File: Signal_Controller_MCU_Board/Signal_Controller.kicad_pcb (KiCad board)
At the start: 2 copper layers, 65 x 75 mm, 53 parts, among them J1 BARREL_JACK, J2 USB_OTG, J3 CONN_02X03, J4 CONN_01X03, J5 CONN_01X02, J6 CONN_01X02, J8 CONN_01X07, Q1 2N7002P,215, Q2 2N7002P,215, Q3 2N7002P,215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

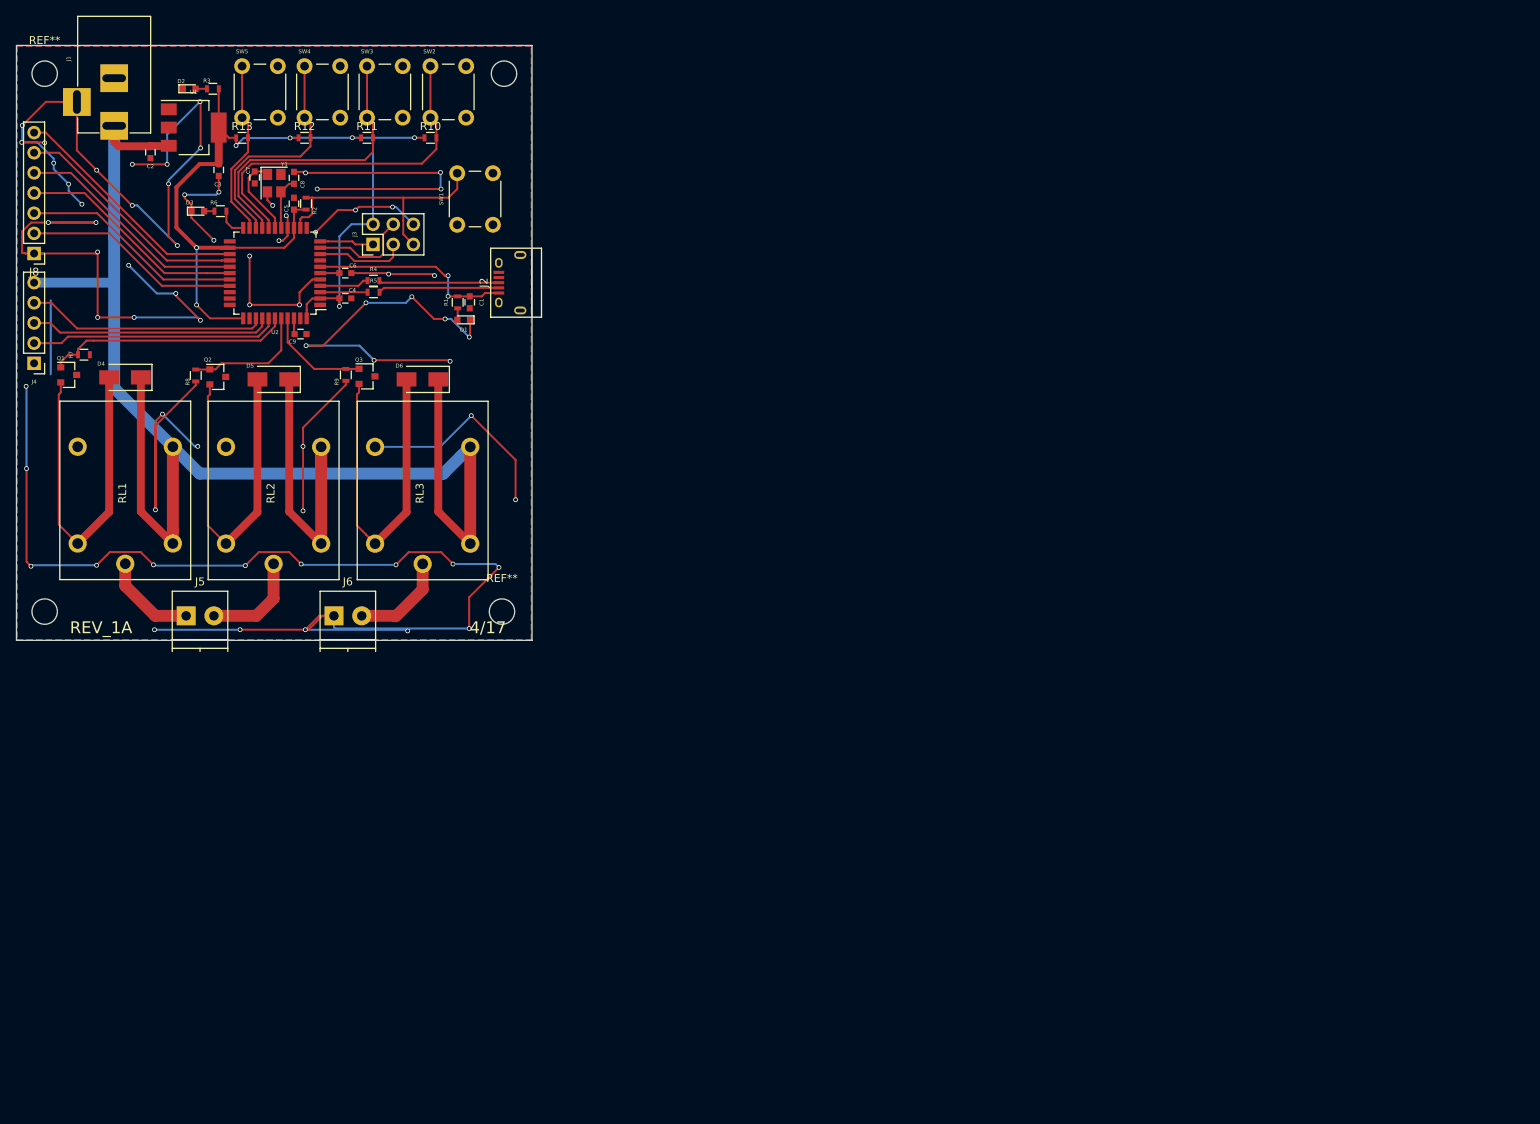
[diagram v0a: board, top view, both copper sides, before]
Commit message: Both boards mostly completed
just need final tweaks, silkscreen stuff etc, all major routing and
placement done
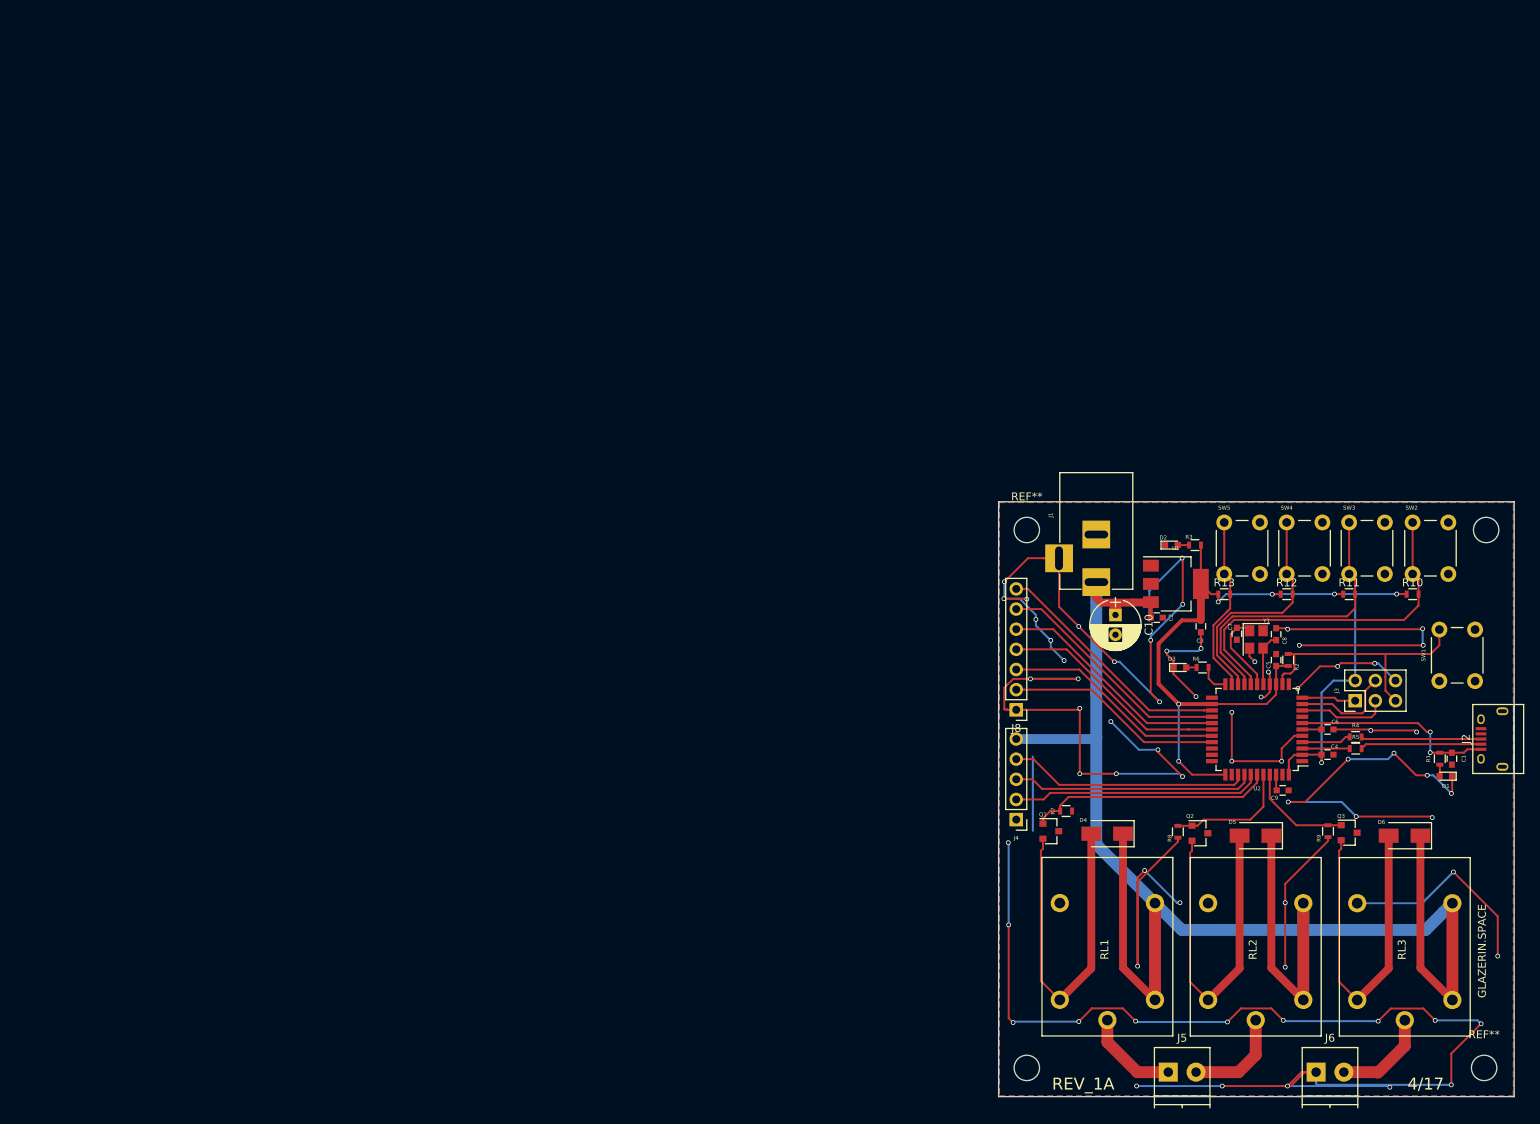
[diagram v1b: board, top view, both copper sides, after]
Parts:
- added C10: CP1, Capacitors_THT:CP_Radial_D6.3mm_P2.50mm, F.Cu at (138.6, 71.8)
- moved C2 139.8 mm to (143.8, 72.1), turned to 0 degrees
- moved ? 136.5 mm to (185.3, 61.1)
- moved ? 136.5 mm to (127.4, 128.9)
- moved C3 136.5 mm to (149.3, 73.2)
- moved C4 136.5 mm to (165.3, 89.4)
- moved C5 136.5 mm to (158.8, 77.5)
- moved C6 136.5 mm to (165.3, 86.2)
- moved C7 136.5 mm to (153.9, 74.2)
- moved C8 136.5 mm to (158.8, 74.2)
- moved C9 136.5 mm to (159.6, 93.9)
- moved D2 136.5 mm to (145.6, 63.0)
- moved D3 136.5 mm to (146.7, 78.4)
- moved D5 136.5 mm to (156.2, 99.6)
- moved D6 136.5 mm to (175.0, 99.6)
- moved J1 136.5 mm to (136.1, 67.7)
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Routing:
- net GND: track 528.0 -> 496.9 mm, vias 69 -> 65
- net (no net): track 9.33 -> 36.0 mm, vias 0 -> 2
- net +12V: track 211.2 -> 214.7 mm
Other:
- board text added: "GLAZERIN.SPACE"

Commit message: I looked at it (minor tweaks)
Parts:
- moved REF** 0.31 mm to (185.3, 129.0)
- moved ? 0.14 mm to (127.3, 129.0)
- moved REF** 0.08 mm to (127.3, 61.0)
- moved ? 0.06 mm to (185.3, 61.0)
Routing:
- net GND: track 496.9 -> 523.6 mm, vias 65 -> 67
- net (no net): track 36.0 -> 9.33 mm, vias 2 -> 0
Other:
- board text added: "BTN_1"
- board text added: "BTN_2"
- board text added: "BTN_3"
- board text added: "BTN_4"
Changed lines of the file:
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@@
   (general
     (links 140)
-    (no_connects 10)
-    (area -0.075001 -0.075001 65.075001 75.075001)
+    (no_connects 2)
+    (area 117.767857 53.433499 194.882143 136.5134)
     (thickness 1.6)
-    (drawings 7)
+    (drawings 11)
     (tracks 529)
     (zones 0)
@@
     (mod_text_size 1 1)
     (mod_text_width 0.15)
-    (pad_size 1.4 1.2)
-    (pad_drill 0)
+    (pad_size 3.2 3.2)
+    (pad_drill 3.2)
     (pad_to_mask_clearance 0.2)
     (aux_axis_origin 0 0)
     (visible_elements 7FFFFFFF)
     (pcbplotparams
-      (layerselection 0x00030_80000001)
-      (usegerberextensions false)
+      (layerselection 0x010ff_80000001)
+      (usegerberextensions true)
       (excludeedgelayer true)
       (linewidth 0.100000)
@@
       (outputformat 1)
       (mirror false)
-      (drillshape 1)
+      (drillshape 0)
       (scaleselection 1)
-      (outputdirectory ""))
+      (outputdirectory Gerbers/))
   )
   (net 0 "")
@@
   )
   (module Mounting_Holes:MountingHole_3.2mm_M3 (layer F.Cu)
-    (at 127.381 61.087)
+    (at 127.325 61.031)
     (descr "Mounting Hole 3.2mm, no annular, M3")
     (tags "mounting hole 3.2mm no annular m3")
@@
     (fp_circle (center 0 0) (end 3.2 0) (layer Cmts.User) (width 0.15))
     (fp_circle (center 0 0) (end 3.45 0) (layer F.CrtYd) (width 0.05))
-    (pad 1 np_thru_hole circle (at 0 0) (size 3.2 3.2) (drill 3.2) (layers *.Cu *.Mask))
+    (pad "" np_thru_hole circle (at -0.056 0) (size 3.2 3.2) (drill 3.2) (layers *.Cu *.Mask))
   )
   (module Mounting_Holes:MountingHole_3.2mm_M3 (layer F.Cu)
-    (at 185.293 61.087)
+    (at 185.325 61.031)
     (descr "Mounting Hole 3.2mm, no annular, M3")
     (tags "mounting hole 3.2mm no annular m3")
@@
   )
   (module Mounting_Holes:MountingHole_3.2mm_M3 (layer F.Cu)
-    (at 185.039 128.905)
+    (at 185.325 129.031)
     (descr "Mounting Hole 3.2mm, no annular, M3")
     (tags "mounting hole 3.2mm no annular m3")
@@
   )
   (module Mounting_Holes:MountingHole_3.2mm_M3 (layer F.Cu)
-    (at 127.381 128.905)
+    (at 127.325 129.031)
     (descr "Mounting Hole 3.2mm, no annular, M3")
     (tags "mounting hole 3.2mm no annular m3")
@@
       (effects (font (size 0.5 0.5) (thickness 0.125)))
     )
-    (fp_text value 1uF (at -1.8415 0 90) (layer F.Fab)
+    (fp_text value 1uF (at -0.7366 1.0668 180) (layer F.Fab)
       (effects (font (size 0.5 0.5) (thickness 0.125)))
     )
@@
     (tags "resistor 0603")
     (attr smd)
-    (fp_text reference R10 (at 0 -1.45) (layer F.SilkS)
-      (effects (font (size 1 1) (thickness 0.15)))
-    )
-    (fp_text value 10K (at 0 1.5) (layer F.Fab)
-      (effects (font (size 1 1) (thickness 0.15)))
+    (fp_text reference R10 (at 0.5588 1.1557) (layer F.SilkS)
+      (effects (font (size 0.5 0.5) (thickness 0.125)))
+    )
+    (fp_text value 10K (at -1.3462 -0.0127 90) (layer F.Fab)
+      (effects (font (size 0.5 0.5) (thickness 0.125)))
     )
     (fp_text user %R (at 0 0) (layer F.Fab)
@@
     (tags "resistor 0603")
     (attr smd)
-    (fp_text reference R11 (at 0 -1.45) (layer F.SilkS)
-      (effects (font (size 1 1) (thickness 0.15)))
-    )
-    (fp_text value 10K (at 0 1.5) (layer F.Fab)
-      (effects (font (size 1 1) (thickness 0.15)))
+    (fp_text reference R11 (at 0.5334 1.1049) (layer F.SilkS)
+      (effects (font (size 0.5 0.5) (thickness 0.125)))
+    )
+    (fp_text value 10K (at -1.27 0.0381 90) (layer F.Fab)
+      (effects (font (size 0.5 0.5) (thickness 0.125)))
     )
     (fp_text user %R (at 0 0) (layer F.Fab)
@@
     (tags "resistor 0603")
     (attr smd)
-    (fp_text reference R12 (at 0 -1.45) (layer F.SilkS)
-      (effects (font (size 1 1) (thickness 0.15)))
-    )
-    (fp_text value 10K (at 0 1.5) (layer F.Fab)
-      (effects (font (size 1 1) (thickness 0.15)))
+    (fp_text reference R12 (at 0.5842 1.1557) (layer F.SilkS)
+      (effects (font (size 0.5 0.5) (thickness 0.125)))
+    )
+    (fp_text value 10K (at -1.2954 0.0127 90) (layer F.Fab)
+      (effects (font (size 0.5 0.5) (thickness 0.125)))
     )
     (fp_text user %R (at 0 0) (layer F.Fab)
@@
     (tags "resistor 0603")
     (attr smd)
-    (fp_text reference R13 (at 0 -1.45) (layer F.SilkS)
-      (effects (font (size 1 1) (thickness 0.15)))
-    )
-    (fp_text value 10K (at 0 1.5) (layer F.Fab)
+    (fp_text reference R13 (at 0.5842 1.1049) (layer F.SilkS)
+      (effects (font (size 0.5 0.5) (thickness 0.125)))
+    )
+    (fp_text value 10K (at -1.3208 -0.0127 90) (layer F.Fab)
       (effects (font (size 0.5 0.5) (thickness 0.125)))
     )
@@
       (effects (font (size 0.5 0.5) (thickness 0.125)))
     )
-    (fp_text value AZ1117IH-5.0TRG1 (at -1.4605 4.064) (layer F.Fab)
+    (fp_text value AZ1117IH-5.0TRG1 (at 0.3302 -3.8989) (layer F.Fab)
       (effects (font (size 0.5 0.5) (thickness 0.125)))
     )
@@
       (effects (font (size 0.5 0.5) (thickness 0.125)))
     )
-    (fp_text value SW_Push (at 3.75 6.7 90) (layer F.Fab)
+    (fp_text value SW_Push (at 3.2893 2.2352 90) (layer F.Fab)
       (effects (font (size 1 1) (thickness 0.15)))
     )
@@
       (effects (font (size 0.5 0.5) (thickness 0.125)))
     )
-    (fp_text value SW_Push (at 3.75 6.7 90) (layer F.Fab)
+    (fp_text value SW_Push (at 3.1369 2.2352 90) (layer F.Fab)
       (effects (font (size 1 1) (thickness 0.15)))
     )
@@
     (descr "CP, Radial series, Radial, pin pitch=2.50mm, , diameter=6.3mm, Electrolytic Capacitor")
     (tags "CP Radial series Radial pin pitch 2.50mm  diameter 6.3mm Electrolytic Capacitor")
-    (fp_text reference C10 (at 1.25 -4.21 270) (layer F.SilkS)
-      (effects (font (size 1 1) (thickness 0.15)))
+    (fp_text reference C10 (at 3.9478 -3.0988 270) (layer F.SilkS)
+      (effects (font (size 0.5 0.5) (thickness 0.125)))
     )
     (fp_text value CP1 (at 1.25 4.21 270) (layer F.Fab)
@@
     )
   )
+  (gr_text BTN_4 (at 155.7274 69.1896) (layer F.SilkS)
+    (effects (font (size 1 1) (thickness 0.25)))
+  )
+  (gr_text BTN_3 (at 163.6268 69.2404) (layer F.SilkS)
+    (effects (font (size 1 1) (thickness 0.25)))
+  )
+  (gr_text BTN_2 (at 171.5008 69.1896) (layer F.SilkS)
+    (effects (font (size 1 1) (thickness 0.25)))
+  )
+  (gr_text BTN_1 (at 179.8066 69.2912) (layer F.SilkS)
+    (effects (font (size 1 1) (thickness 0.25)))
+  )
   (gr_text GLAZERIN.SPACE (at 184.785 114.173 90) (layer F.SilkS)
     (effects (font (size 1 1) (thickness 0.25)))
@@
   (gr_line (start 123.825 57.531) (end 123.825 132.531) (angle 90) (layer Edge.Cuts) (width 0.15))
   (segment (start 128.143 89.662) (end 128.143 98.9965) (width 0.25) (layer B.Cu) (net 0))
-  (segment (start 181.1655 104.2035) (end 186.7535 109.7915) (width 0.25) (layer F.Cu) (net 0))
-  (segment (start 186.7535 109.7915) (end 186.7535 114.808) (width 0.25) (layer F.Cu) (net 0))
-  (via (at 186.7535 114.808) (size 0.6) (drill 0.4) (layers F.Cu B.Cu) (net 0))
-  (segment (start 169.037 108.1405) (end 177.2285 108.1405) (width 0.25) (layer B.Cu) (net 0))
-  (segment (start 177.2285 108.1405) (end 181.1655 104.2035) (width 0.25) (layer B.Cu) (net 0))
-  (via (at 181.1655 104.2035) (size 0.6) (drill 0.4) (layers F.Cu B.Cu) (net 0))
   (segment (start 162.1155 85.433) (end 176.702736 85.433) (width 0.25) (layer F.Cu) (net 1))
   (segment (start 176.702736 85.433) (end 177.820236 86.5505) (width 0.25) (layer F.Cu) (net 1))
@@
   (segment (start 180.975 89.166) (end 182.487 89.166) (width 0.25) (layer F.Cu) (net 1))
   (segment (start 179.451 89.166) (end 180.975 89.166) (width 0.25) (layer F.Cu) (net 1))
+  (segment (start 181.1655 104.2035) (end 186.7535 109.7915) (width 0.25) (layer F.Cu) (net 2))
+  (segment (start 186.7535 109.7915) (end 186.7535 114.808) (width 0.25) (layer F.Cu) (net 2))
+  (via (at 186.7535 114.808) (size 0.6) (drill 0.4) (layers F.Cu B.Cu) (net 2))
+  (segment (start 169.037 108.1405) (end 177.2285 108.1405) (width 0.25) (layer B.Cu) (net 2))
+  (segment (start 177.2285 108.1405) (end 181.1655 104.2035) (width 0.25) (layer B.Cu) (net 2))
+  (via (at 181.1655 104.2035) (size 0.6) (drill 0.4) (layers F.Cu B.Cu) (net 2))
   (segment (start 146.9644 64.6176) (end 142.8242 68.7578) (width 0.25) (layer B.Cu) (net 2))
   (segment (start 142.8242 68.7578) (end 142.8242 72.517) (width 0.25) (layer B.Cu) (net 2))

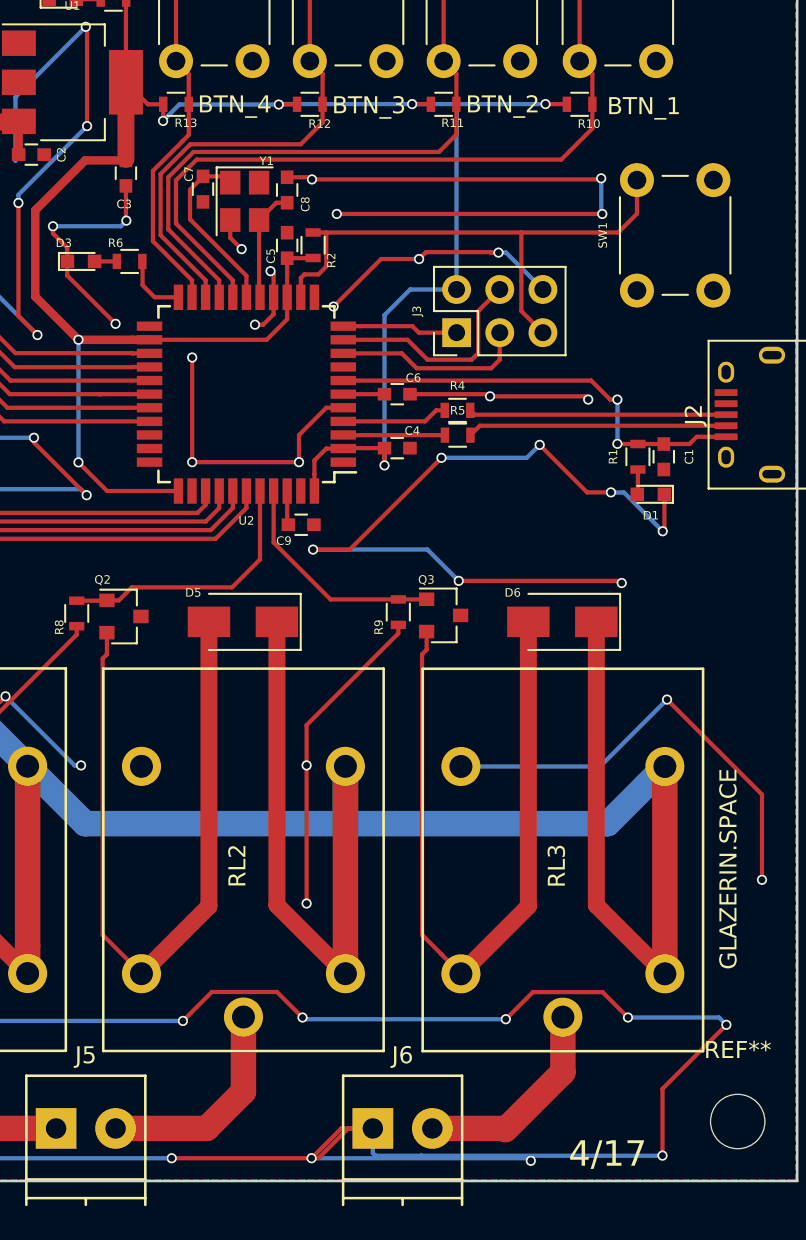
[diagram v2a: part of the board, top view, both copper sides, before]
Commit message: breaking out a UART instead of just 6 GPIO
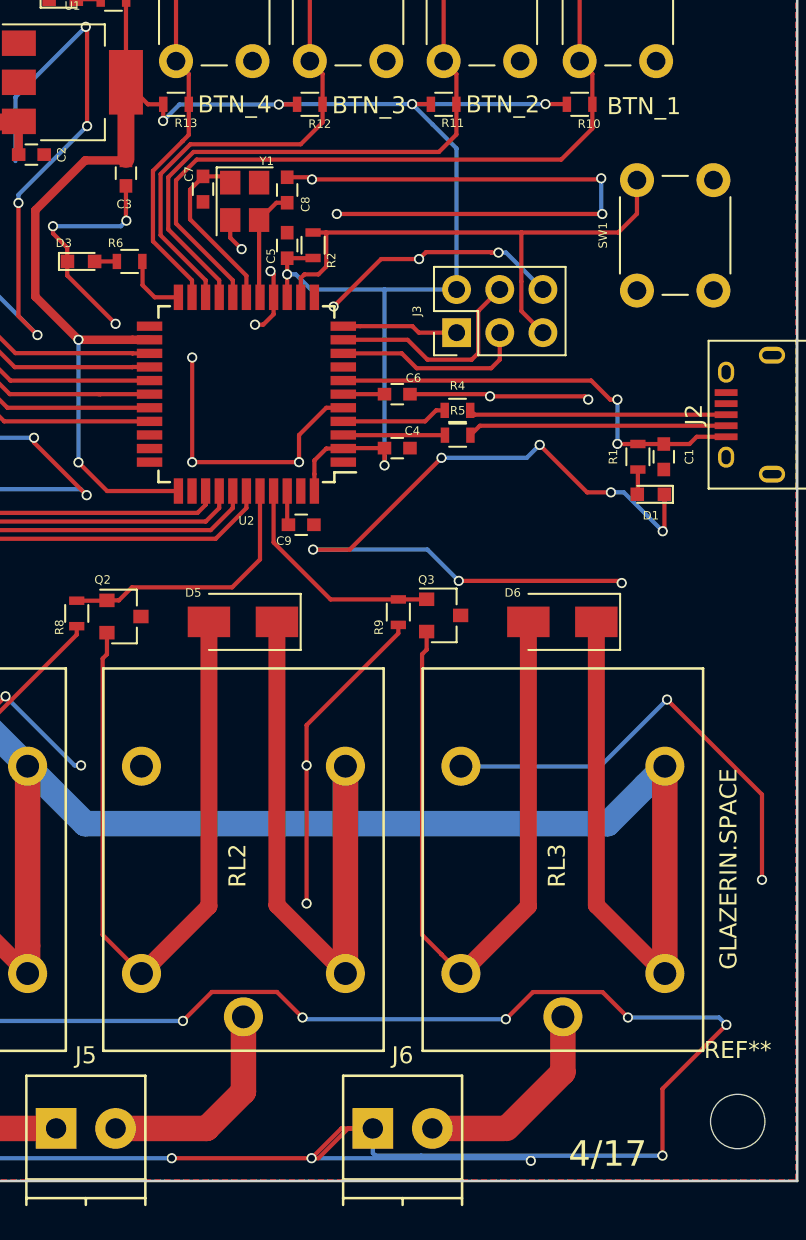
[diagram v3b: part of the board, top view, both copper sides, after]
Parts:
- C1: value 10uF -> 1uF
- C9: value 0.1uF -> 1uF
- R1, R3, R6: value R -> 1K
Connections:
- J8 pad 2: /GPIO_6 -> /GPIO_4
- J8 pad 3: /GPIO_5 -> /GPIO_3
- J8 pad 4: /GPIO_4 -> /GPIO_2
- J8 pad 5: /GPIO_3 -> /GPIO_1
- J8 pad 6: /GPIO_2 -> /TXO
- J8 pad 7: /GPIO_1 -> /RXI
- U1 pad 4: +5V -> (no net)
- U2 pad 20: /BUTTON_3 -> /RXI
- U2 pad 21: /BUTTON_4 -> /TXO
- U2 pad 25: /GPIO_1 -> /BUTTON_3
- U2 pad 26: /GPIO_2 -> /BUTTON_4
- U2 pad 27: /GPIO_3 -> /GPIO_1
- U2 pad 28: /GPIO_4 -> /GPIO_2
- U2 pad 29: /GPIO_5 -> /GPIO_3
- U2 pad 30: /GPIO_6 -> /GPIO_4
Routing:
- net /GPIO_5: track 28.1 -> 0.00 mm
- net /GPIO_6: track 27.4 -> 0.00 mm
- net /BUTTON_4: track 22.5 -> 48.7 mm
- net /RXI: track 0.00 -> 20.6 mm
- net /BUTTON_3: track 29.8 -> 40.2 mm
- net /TXO: track 0.00 -> 4.15 mm
- net GND: track 523.6 -> 521.6 mm, vias 67 -> 66
- net Net-(C8-Pad2): track 6.64 -> 8.63 mm, vias 0 -> 1
- net +5V: track 118.4 -> 116.6 mm, vias 7 -> 8
- net /GPIO_4: track 29.0 -> 27.4 mm
- net /GPIO_1: track 31.0 -> 29.6 mm
- net /GPIO_3: track 29.6 -> 28.1 mm
- net /GPIO_2: track 30.3 -> 29.0 mm
